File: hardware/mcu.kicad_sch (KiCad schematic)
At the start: 21 parts, among them J2 Debug, SW1 RESET, SW2 BOOT, U1 STM32F405RGTx, Y1 8MHz

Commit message: Define footprints
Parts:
- C1, C10, C11, C12, C13, C2, C3, C4, C5, C6, C7, C8, C9: footprint (none) -> Capacitor_SMD:C_0402_1005Metric
- L1: footprint (none) -> Inductor_SMD:L_0402_1005Metric
- R1, R2: footprint (none) -> Resistor_SMD:R_0402_1005Metric
- SW1, SW2: footprint (none) -> Button_Switch_SMD:SW_Push_SPST_NO_Alps_SKRK; LCSC (none) -> C720477
- Y1: footprint (none) -> Crystal:Crystal_SMD_3225-4Pin_3.2x2.5mm
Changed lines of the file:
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@@
 			)
 		)
-		(property "Footprint" ""
+		(property "Footprint" "Inductor_SMD:L_0402_1005Metric"
 			(at 118.11 29.21 0)
 			(effects
@@
 			)
 		)
-		(property "Footprint" ""
+		(property "Footprint" "Button_Switch_SMD:SW_Push_SPST_NO_Alps_SKRK"
 			(at 60.96 48.26 0)
 			(effects
@@
 			)
 		)
+		(property "LCSC" "C720477"
+			(at 66.04 48.26 90)
+			(effects
+				(font
+					(size 1.27 1.27)
+				)
+				(hide yes)
+			)
+		)
 		(pin "2"
 		)
@@
 			)
 		)
-		(property "Footprint" ""
+		(property "Footprint" "Capacitor_SMD:C_0402_1005Metric"
 			(at 54.3052 80.01 0)
 			(effects
@@
 			)
 		)
-		(property "Footprint" ""
+		(property "Footprint" "Button_Switch_SMD:SW_Push_SPST_NO_Alps_SKRK"
 			(at 48.26 67.31 0)
 			(effects
@@
 			)
 		)
+		(property "LCSC" "C720477"
+			(at 53.34 67.31 90)
+			(effects
+				(font
+					(size 1.27 1.27)
+				)
+				(hide yes)
+			)
+		)
 		(pin "2"
 		)
@@
 			)
 		)
-		(property "Footprint" ""
+		(property "Footprint" "Capacitor_SMD:C_0402_1005Metric"
 			(at 190.1952 36.83 0)
 			(effects
@@
 			)
 		)
-		(property "Footprint" ""
+		(property "Footprint" "Capacitor_SMD:C_0402_1005Metric"
 			(at 177.4952 36.83 0)
 			(effects
@@
 			)
 		)
-		(property "Footprint" ""
+		(property "Footprint" "Crystal:Crystal_SMD_3225-4Pin_3.2x2.5mm"
 			(at 102.87 78.74 0)
 			(effects
@@
 			)
 		)
-		(property "Footprint" ""
+		(property "Footprint" "Capacitor_SMD:C_0402_1005Metric"
 			(at 164.7952 36.83 0)
 			(effects
@@
 			)
 		)
-		(property "Footprint" ""
+		(property "Footprint" "Capacitor_SMD:C_0402_1005Metric"
 			(at 140.6652 36.83 0)
 			(effects
@@
 			)
 		)
-		(property "Footprint" ""
+		(property "Footprint" "Capacitor_SMD:C_0402_1005Metric"
 			(at 127.9652 36.83 0)
 			(effects
@@
 			)
 		)
-		(property "Footprint" ""
+		(property "Footprint" "Capacitor_SMD:C_0402_1005Metric"
 			(at 91.44 81.28 0)
 			(effects
@@
 			)
 		)
-		(property "Footprint" ""
+		(property "Footprint" "Capacitor_SMD:C_0402_1005Metric"
 			(at 152.0952 36.83 0)
 			(effects
@@
 			)
 		)
-		(property "Footprint" ""
+		(property "Footprint" "Capacitor_SMD:C_0402_1005Metric"
 			(at 110.49 81.28 0)
 			(effects
@@
 			)
 		)
-		(property "Footprint" ""
+		(property "Footprint" "Capacitor_SMD:C_0402_1005Metric"
 			(at 54.3052 50.8 0)
 			(effects
@@
 			)
 		)
-		(property "Footprint" ""
+		(property "Footprint" "Capacitor_SMD:C_0402_1005Metric"
 			(at 129.2352 134.62 0)
 			(effects
@@
 			)
 		)
-		(property "Footprint" ""
+		(property "Footprint" "Resistor_SMD:R_0402_1005Metric"
 			(at 64.262 76.2 90)
 			(effects
@@
 			)
 		)
-		(property "Footprint" ""
+		(property "Footprint" "Capacitor_SMD:C_0402_1005Metric"
 			(at 202.8952 36.83 0)
 			(effects
@@
 			)
 		)
-		(property "Footprint" ""
+		(property "Footprint" "Capacitor_SMD:C_0402_1005Metric"
 			(at 117.8052 134.62 0)
 			(effects
@@
 			)
 		)
-		(property "Footprint" ""
+		(property "Footprint" "Resistor_SMD:R_0402_1005Metric"
 			(at 51.562 38.1 90)
 			(effects

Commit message: MCU layout
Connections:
- net BOOT: now also C13.2; no longer C13.1
- net GND: no longer C13.2
- net VDDA: now also U1.13 (VDDA)
- net +3.3V: now reaches L1.1
- net +3.3V: now also C13.1, C3.1, C4.1, C5.1, C6.1, C7.1, J2.1 (VTref), R1.1, SW2.2, U1.1 (VBAT), U1.19 (VDD), U1.32 (VDD), U1.48 (VDD), U1.64 (VDD)
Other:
- moved on the sheet: C10, C13, R1, R2, SW1, SW2

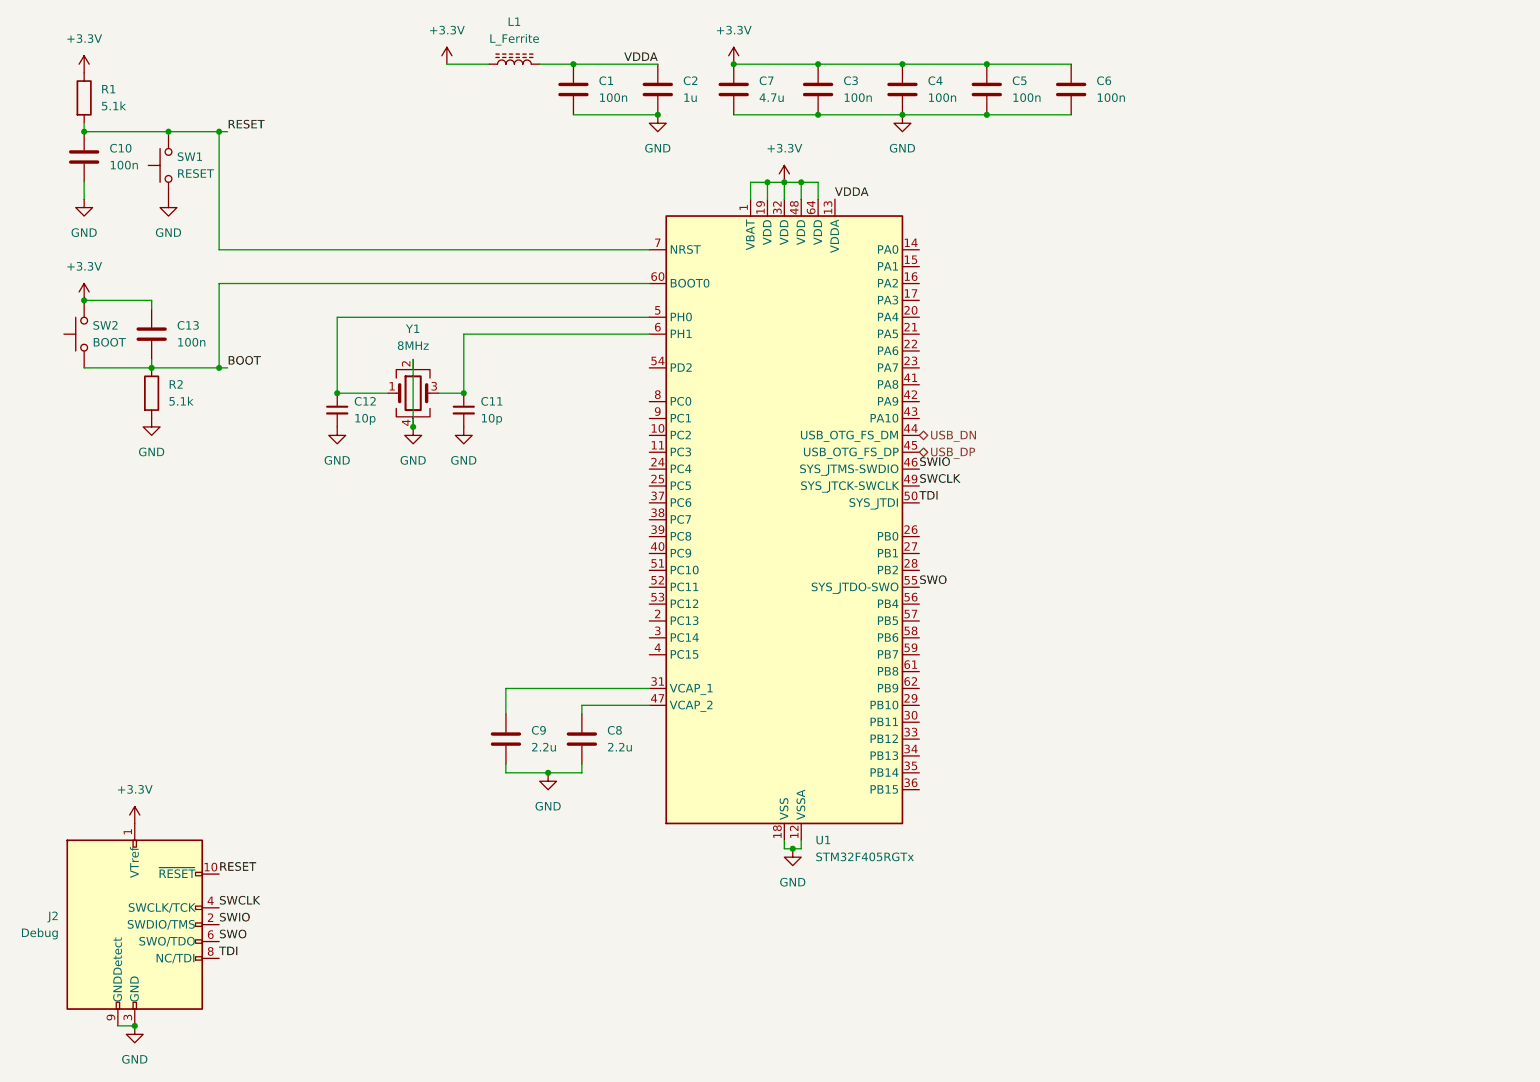
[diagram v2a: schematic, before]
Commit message: Added power connector
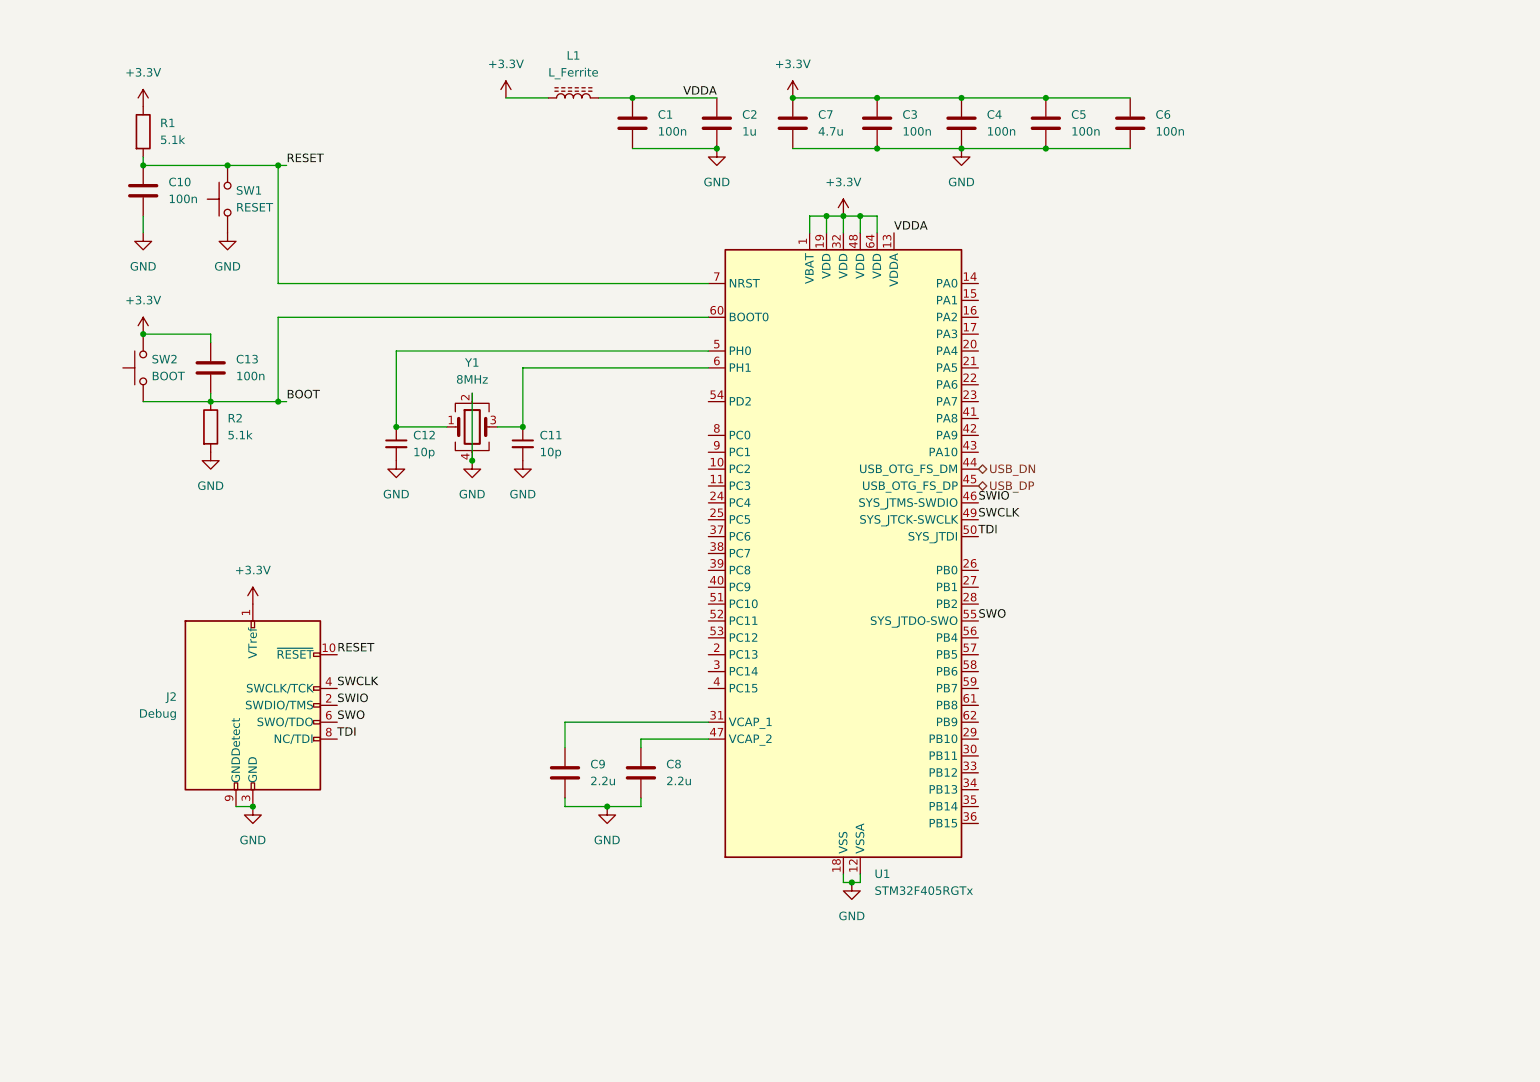
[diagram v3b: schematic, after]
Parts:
- U1: LCSC (none) -> C15742
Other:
- moved on the sheet: C1, C10, C11, C12, C13, C2, C3, C4, C5, C6, C7, C8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

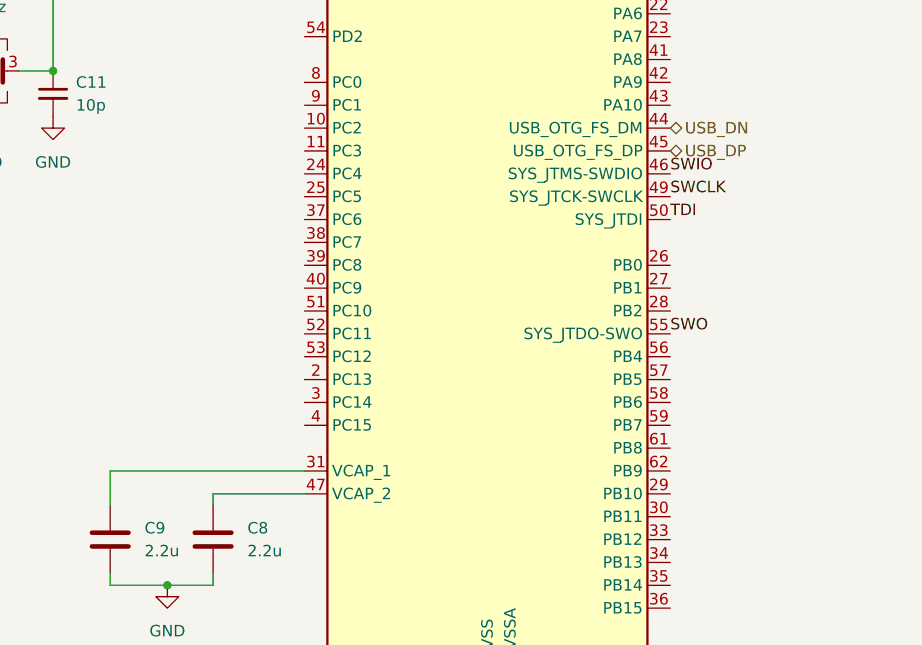
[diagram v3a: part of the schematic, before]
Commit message: Add CAN, USB and sensors
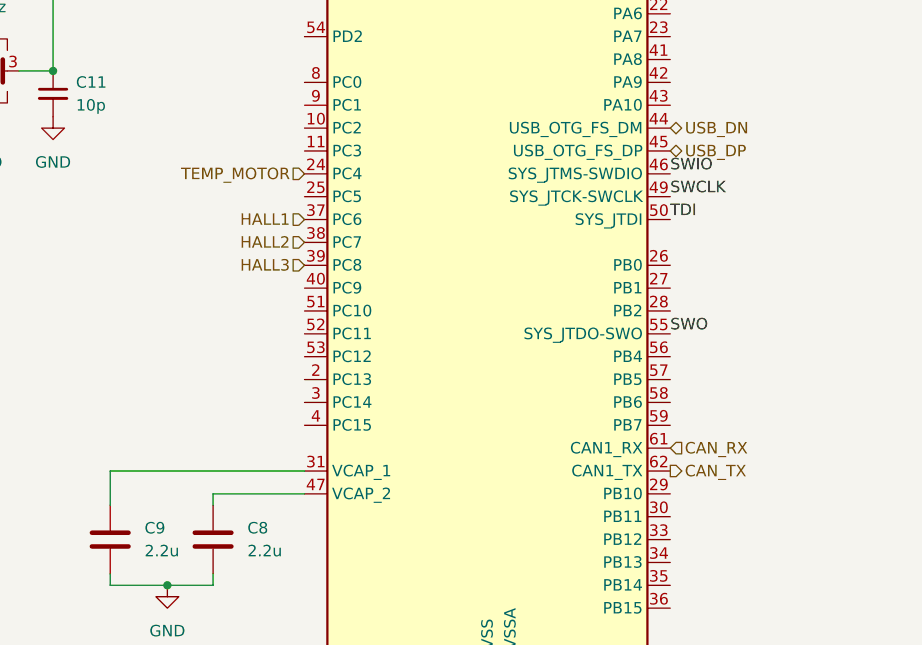
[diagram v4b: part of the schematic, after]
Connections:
- net TEMP_MOTOR: now reaches U1.24 (PC4)
- net HALL1: now reaches U1.37 (PC6)
- net HALL2: now reaches U1.38 (PC7)
- net HALL3: now reaches U1.39 (PC8)
- net CAN_RX: now reaches U1.61 (PB8)
- net CAN_TX: now reaches U1.62 (PB9)
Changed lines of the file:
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@@
+		)
+	)
+	(hierarchical_label "CAN_RX"
+		(shape input)
+		(at 187.96 125.73 0)
+		(effects
+			(font
+				(size 1.27 1.27)
+			)
+			(justify left)
+		)
+	)
+	(hierarchical_label "HALL2"
+		(shape input)
+		(at 147.32 102.87 180)
+		(effects
+			(font
+				(size 1.27 1.27)
+			)
+			(justify right)
 		)
 	)
@@
 		)
 	)
+	(hierarchical_label "HALL3"
+		(shape input)
+		(at 147.32 105.41 180)
+		(effects
+			(font
+				(size 1.27 1.27)
+			)
+			(justify right)
+		)
+	)
 	(hierarchical_label "USB_DP"
 		(shape bidirectional)
@@
 		)
 	)
+	(hierarchical_label "HALL1"
+		(shape input)
+		(at 147.32 100.33 180)
+		(effects
+			(font
+				(size 1.27 1.27)
+			)
+			(justify right)
+		)
+	)
+	(hierarchical_label "TEMP_MOTOR"
+		(shape input)
+		(at 147.32 95.25 180)
+		(effects
+			(font
+				(size 1.27 1.27)
+			)
+			(justify right)
+		)
+	)
+	(hierarchical_label "CAN_TX"
+		(shape output)
+		(at 187.96 128.27 0)
+		(effects
+			(font
+				(size 1.27 1.27)
+			)
+			(justify left)
+		)
+	)
 	(symbol
 		(lib_id "Device:L_Ferrite")
@@
 		)
 		(pin "62"
+			(alternate "CAN1_TX")
 		)
 		(pin "27"
@@
 		)
 		(pin "61"
+			(alternate "CAN1_RX")
 		)
 		(pin "29"

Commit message: half bridges
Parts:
- renumbered C8 to C10, C2 to C11, C7 to C12, C3 to C13, C4 to C14, C5 to C15, C6 to C16, C10 to C4, C13 to C5, C12 to C6, C11 to C7, C9 to C8, C1 to C9, J2 to J6, R1 to R15, R2 to R16, SW2 to SW1, SW1 to SW2, U1 to U2
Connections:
- net I3: now reaches U2.10 (PC2)
- net Vin: now reaches U2.11 (PC3)
- net V1: now reaches U2.14 (PA0)
- net V2: now reaches U2.15 (PA1)
- net V3: now reaches U2.16 (PA2)
- net T1: now reaches U2.17 (PA3)
- net T2: now reaches U2.26 (PB0)
- net T3: now reaches U2.27 (PB1)
- net L1: now reaches U2.34 (PB13)
- net L2: now reaches U2.35 (PB14)
- net L3: now reaches U2.36 (PB15)
- net H1: now reaches U2.41 (PA8)
- net H2: now reaches U2.42 (PA9)
- net H3: now reaches U2.43 (PA10)
- net LED_GREEN: now reaches U2.57 (PB5)
- net LED_RED: now reaches U2.59 (PB7)
- net I1: now reaches U2.8 (PC0)
- net I2: now reaches U2.9 (PC1)

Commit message: Power Layout
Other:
- title: (none) -> GreenMobi Drive
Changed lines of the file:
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@@
 	(generator_version "9.0")
 	(paper "A4")
+	(title_block
+		(title "GreenMobi Drive")
+		(date "2025-07-02")
+		(rev "0.1")
+	)
 	(junction
 		(at 82.55 80.01)

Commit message: Layout
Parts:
- added H1, H2, H3, H4, H5: Heatsink, MountingHole:MountingHole_3.2mm_M3_Pad, symbol Mechanical:MountingHole_Pad
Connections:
- net GND: now also H1.1, H2.1, H3.1, H4.1, H5.1
